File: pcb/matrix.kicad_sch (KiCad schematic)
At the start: 177 parts, among them SW10 MX_Switch, SW11 MX_Switch, SW12 MX_Switch, SW13 MX_Switch, SW14 MX_Switch, SW15 MX_Switch, SW16 MX_Switch, SW17 MX_Switch, SW18 MX_Switch, SW19 MX_Switch, SW20 MX_Switch, SW21 MX_Switch, SW22 MX_Switch, SW23 MX_Switch, SW24 MX_Switch, SW25 MX_Switch, SW26 MX_Switch, SW27 MX_Switch, SW28 MX_Switch, SW29 MX_Switch, SW30 MX_Switch, SW31 MX_Switch, SW32 MX_Switch, SW33 MX_Switch, SW34 MX_Switch, SW35 MX_Switch, SW36 MX_Switch, SW37 MX_Switch, SW38 MX_Switch, SW39 MX_Switch, SW4 MX_Switch, SW40 MX_Switch, SW41 MX_Switch, SW42 MX_Switch, SW43 MX_Switch, SW44 MX_Switch, SW45 MX_Switch, SW46 MX_Switch, SW47 MX_Switch, SW48 MX_Switch, SW49 MX_Switch, SW5 MX_Switch, SW50 MX_Switch, SW51 MX_Switch, SW52 MX_Switch, SW53 MX_Switch, SW54 MX_Switch, SW55 MX_Switch, SW56 MX_Switch, SW57 MX_Switch, SW58 MX_Switch, SW59 MX_Switch, SW6 MX_Switch, SW60 MX_Switch, SW61 MX_Switch, SW62 MX_Switch, SW63 MX_Switch, SW64 MX_Switch, SW65 MX_Switch, SW66 MX_Switch, SW67 MX_Switch, SW69 MX_Switch, SW7 MX_Switch, SW70 MX_Switch, SW71 MX_Switch, SW72 MX_Switch, SW73 MX_Switch, SW74 MX_Switch, SW75 MX_Switch, SW76 MX_Switch, SW77 MX_Switch, SW78 MX_Switch, SW79 MX_Switch, SW8 MX_Switch, SW80 MX_Switch, SW81 MX_Switch, SW82 MX_Switch, SW83 MX_Switch, SW84 MX_Switch, SW85 MX_Switch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

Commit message: Touch up silkscreen and schematic
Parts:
- SW10, SW81: footprint Switch_Keyboard_Kailh:SW_Hotswap_Kailh_MX_plated_1.50u -> Switch_Keyboard_Kailh:SW_Hotswap_Kailh_MX_1.50u
- SW12, SW77: footprint Switch_Keyboard_Kailh:SW_Hotswap_Kailh_MX_plated_2.25u -> Switch_Keyboard_Kailh:SW_Hotswap_Kailh_MX_2.25u
- SW13, SW19, SW56, SW62, SW91: footprint Switch_Keyboard_Kailh:SW_Hotswap_Kailh_MX_plated_1.25u -> Switch_Keyboard_Kailh:SW_Hotswap_Kailh_MX_1.25u
- SW14, SW15, SW16, SW17, SW18, SW20, SW21, SW22, SW23, SW24, SW25, SW26, SW27, SW28, SW29, SW30, SW31, SW32, SW33, SW34, SW35, SW36, SW37, SW38, SW39, SW4, SW41, SW42, SW43, SW44, SW45, SW46, SW47, SW48, SW49, SW5, SW50, SW51, SW52, SW53, SW54, SW55, SW57, SW58, SW59, SW6, SW60, SW61, SW63, SW64, SW65, SW66, SW67, SW69, SW7, SW70, SW71, SW72, SW74, SW75, SW76, SW78, SW79, SW8, SW82, SW83, SW85, SW86, SW87, SW88, SW89, SW9: footprint Switch_Keyboard_Kailh:SW_Hotswap_Kailh_MX_plated_1.00u -> Switch_Keyboard_Kailh:SW_Hotswap_Kailh_MX_1.00u
- SW40: footprint Switch_Keyboard_Kailh:SW_Hotswap_Kailh_MX_plated_6.25u -> Switch_Keyboard_Kailh:SW_Hotswap_Kailh_MX_6.25u
- SW73: footprint Switch_Keyboard_Kailh:SW_Hotswap_Kailh_MX_plated_1.75u -> Switch_Keyboard_Kailh:SW_Hotswap_Kailh_MX_1.75u
- SW80: footprint Switch_Keyboard_Kailh:SW_Hotswap_Kailh_MX_plated_2.00u -> Switch_Keyboard_Kailh:SW_Hotswap_Kailh_MX_2.00u

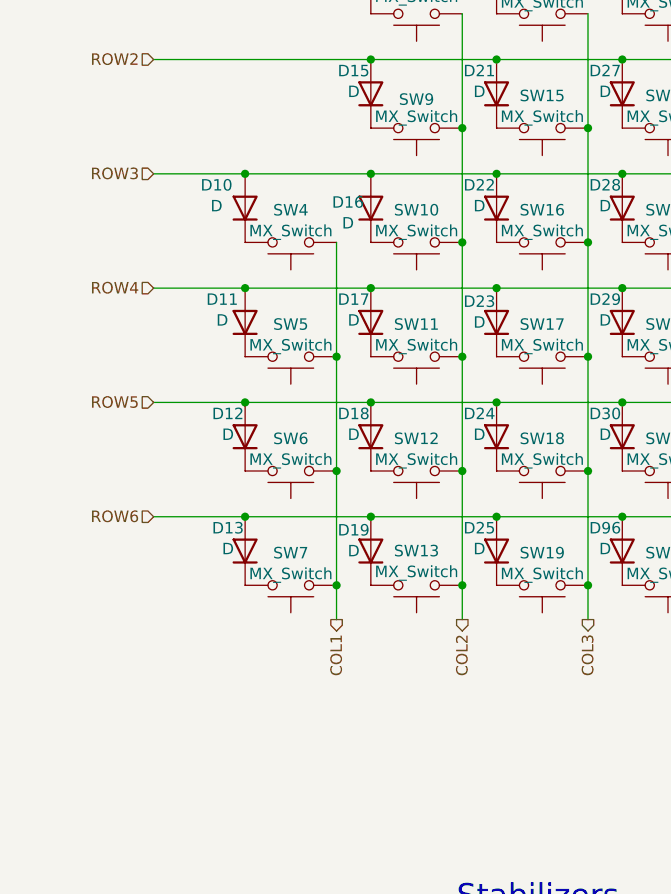
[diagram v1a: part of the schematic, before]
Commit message: Make caps lock footprint two separate symbols and footprints
...so that JLCPCB will actually solder them both
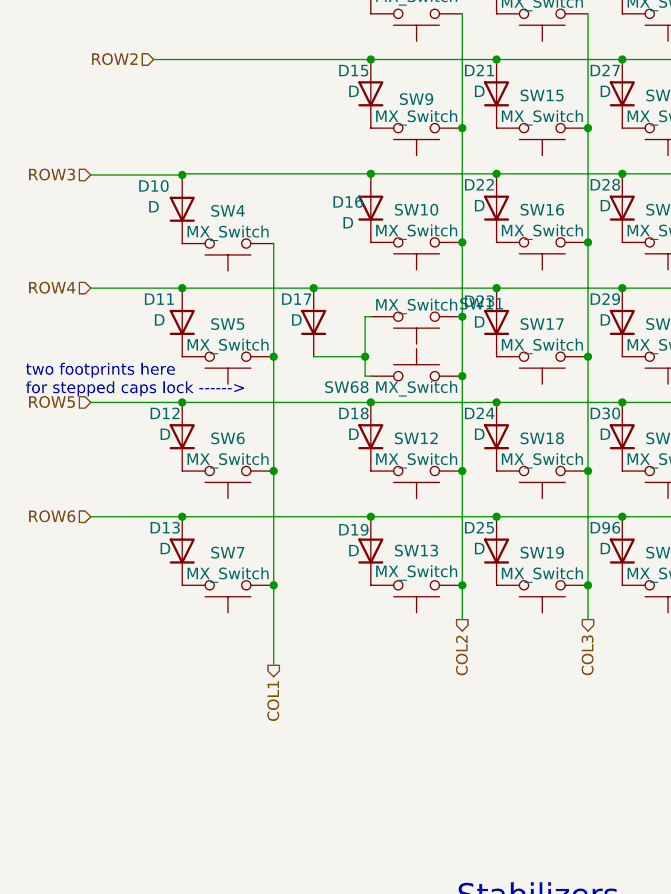
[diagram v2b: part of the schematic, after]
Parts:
- added SW68: MX_Switch, Switch_Keyboard_Kailh:SW_Hotswap_Kailh_MX, symbol Switch:SW_Push
- SW11: footprint Switch_Keyboard_Kailh:SW_Hotswap_Kailh_MX_1.75u_SteppedCapsLock -> Switch_Keyboard_Kailh:SW_Hotswap_Kailh_MX_1.75u
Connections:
- net COL2: now also SW11.2, SW68.1; no longer SW11.1
- net at D17.1 (K): now also SW11.1, SW68.2; no longer SW11.2
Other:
- note added: "two footprints here for stepped caps lock ------>"
- moved on the sheet: D10, D11, D12, D13, D17, SW11, SW4, SW5, SW6, SW7
